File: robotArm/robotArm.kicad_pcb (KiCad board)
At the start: 4 copper layers, 127 x 66 mm, 30 parts, among them J1 Barrel_Jack, J2 Conn_01x16_Pin, J3 Conn_01x04, J4 Conn_01x04, J5 Conn_01x04, J6 Conn_01x04, U2 TMC2209_SILENTSTEPSTICK, U4 TMC2209_SILENTSTEPSTICK, U5 TMC2209_SILENTSTEPSTICK, U6 74HC165

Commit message: First Real Cleanup
First real cleanup
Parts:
- added D10: ST1, LED_THT:LED_D3.0mm_FlatTop, F.Cu at (138.4, 64.8)
- added D11: ST2, LED_THT:LED_D3.0mm_FlatTop, F.Cu at (133.3, 64.8)
- added D12: ST3, LED_THT:LED_D3.0mm_FlatTop, F.Cu at (128.3, 64.8)
- added D13: USR0, LED_THT:LED_D3.0mm_FlatTop, F.Cu at (123.2, 64.8)
- added D14: USR1, LED_THT:LED_D3.0mm_FlatTop, F.Cu at (118.1, 64.8)
- added D15: USR2, LED_THT:LED_D3.0mm_FlatTop, F.Cu at (113.0, 64.8)
- added D16: USR3, LED_THT:LED_D3.0mm_FlatTop, F.Cu at (108.0, 64.8)
- added D9: ST0, LED_THT:LED_D3.0mm_FlatTop, F.Cu at (143.5, 64.8)
- added R10: 330, Resistor_THT:R_Box_L8.4mm_W2.5mm_P5.08mm, F.Cu at (144.8, 74.9)
- added R11: 330, Resistor_THT:R_Box_L8.4mm_W2.5mm_P5.08mm, F.Cu at (139.7, 74.9)
- added R12: 330, Resistor_THT:R_Box_L8.4mm_W2.5mm_P5.08mm, F.Cu at (134.6, 74.9)
- added R13: 330, Resistor_THT:R_Box_L8.4mm_W2.5mm_P5.08mm, F.Cu at (129.5, 74.9)
- added R14: 330, Resistor_THT:R_Box_L8.4mm_W2.5mm_P5.08mm, F.Cu at (124.5, 69.8)
- added R15: 330, Resistor_THT:R_Box_L8.4mm_W2.5mm_P5.08mm, F.Cu at (119.4, 69.9)
- added R16: 330, Resistor_THT:R_Box_L8.4mm_W2.5mm_P5.08mm, F.Cu at (114.3, 69.8)
- added R17: 330, Resistor_THT:R_Box_L8.4mm_W2.5mm_P5.08mm, F.Cu at (109.2, 74.9)
- D5: value D5 -> IX1
- R2: value R -> 330
- moved U7 6.48 mm to (88.4, 89.4)
- moved J2 5.08 mm to (147.3, 78.7)
- moved U4 3.81 mm to (130.8, 83.8)
- moved U5 2.54 mm to (130.8, 108.0)
- moved U6 2.54 mm to (106.7, 83.8)
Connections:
- J2 pad 1: D0 -> ES0
- J2 pad 11: D5 -> USR1
- J2 pad 13: D6 -> USR2
- J2 pad 15: D7 -> USR3
- J2 pad 3: D1 -> ES1
- J2 pad 5: D2 -> ES2
- J2 pad 7: D3 -> ES3
- J2 pad 9: D4 -> USR0
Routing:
- net +3.3V: track 313.4 -> 236.0 mm, vias 0 -> 1
- net D0: track 48.0 -> 0.00 mm, vias 1 -> 0
- net DIR_2: track 64.2 -> 105.4 mm, vias 1 -> 0
- net D1: track 40.5 -> 0.00 mm, vias 1 -> 0
- net D2: track 34.2 -> 0.00 mm, vias 1 -> 0
- net D4: track 29.4 -> 0.00 mm, vias 1 -> 0
- net D3: track 28.8 -> 0.00 mm
- net D5: track 27.5 -> 0.00 mm, vias 1 -> 0
- net D7: track 24.1 -> 0.00 mm
- net D6: track 23.3 -> 0.00 mm
- net +12V: track 182.6 -> 167.4 mm
- net /M2-2A: track 6.89 -> 19.1 mm
- net /M4-1A: track 17.7 -> 6.35 mm
- net CLK: track 49.2 -> 38.2 mm, vias 1 -> 0
- net Net-(D9-K): track 0.00 -> 10.7 mm
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- added copper zone on In1.Cu, net +3.3V
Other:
- board size 127 x 66 mm -> 127 x 69.9 mm

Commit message: Attempt 2.1
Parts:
- removed D10: ST1, LED_THT:LED_D3.0mm_FlatTop
- removed D11: ST2, LED_THT:LED_D3.0mm_FlatTop
- removed D12: ST3, LED_THT:LED_D3.0mm_FlatTop
- removed D13: USR0, LED_THT:LED_D3.0mm_FlatTop
- removed D14: USR1, LED_THT:LED_D3.0mm_FlatTop
- removed D15: USR2, LED_THT:LED_D3.0mm_FlatTop
- removed D16: USR3, LED_THT:LED_D3.0mm_FlatTop
- added C1: 47μ, Capacitor_THT:CP_Radial_D5.0mm_P2.50mm, F.Cu at (113.7, 60.3)
- added C2: 47μ, Capacitor_THT:CP_Radial_D5.0mm_P2.50mm, F.Cu at (134.7, 128.9)
- added C3: 47μ, Capacitor_THT:CP_Radial_D5.0mm_P2.50mm, F.Cu at (136.0, 67.3)
- added C4: 100μ, Capacitor_THT:CP_Radial_D7.5mm_P2.50mm, F.Cu at (57.8, 69.8)
- added C5: 47μ, Capacitor_THT:CP_Radial_D5.0mm_P2.50mm, F.Cu at (137.2, 97.8)
- added SW1: SW_DIP_x08, Package_DIP:DIP-16_W7.62mm, F.Cu at (95.3, 109.2)
- added SW2: SW_SPDT, Library:SS-12D10G5_XKB, F.Cu at (41.9, 71.1)
- added U3: 74HC245, Package_DIP:DIP-20_W7.62mm, F.Cu at (140.3, 94.6)
- added U9: 74LS279, Package_DIP:DIP-16_W7.62mm, F.Cu at (140.3, 121.3)
- D1: value DIAG1 -> USR3; footprint LED_THT:LED_D3.0mm_FlatTop -> LED_THT:LED_D5.0mm
- D2: value DIAG2 -> USR2; footprint LED_THT:LED_D3.0mm_FlatTop -> LED_THT:LED_D5.0mm
- D3: value DIAG3 -> USR1; footprint LED_THT:LED_D3.0mm_FlatTop -> LED_THT:LED_D5.0mm
- D4: value DIAG4 -> USR0; footprint LED_THT:LED_D3.0mm_FlatTop -> LED_THT:LED_D5.0mm
- D5: value IX1 -> ES3; footprint LED_THT:LED_D3.0mm_FlatTop -> LED_THT:LED_D5.0mm
- D6: value IX2 -> ES2; footprint LED_THT:LED_D3.0mm_FlatTop -> LED_THT:LED_D5.0mm
- D7: value IX3 -> ES1; footprint LED_THT:LED_D3.0mm_FlatTop -> LED_THT:LED_D5.0mm
- D8: value IX4 -> ES0; footprint LED_THT:LED_D3.0mm_FlatTop -> LED_THT:LED_D5.0mm
- D9: value ST0 -> LED; footprint LED_THT:LED_D3.0mm_FlatTop -> LED_THT:LED_D5.0mm_Clear
- J2: value Conn_01x16_Pin -> ENDSTOP INPUTS
- J3: value Conn_01x04 -> STEPPER1
- J4: value Conn_01x04 -> STEPPER4
- J5: value Conn_01x04 -> STEPPER2
- J6: value Conn_01x04 -> STEPPER3
- R1: value R -> 470 Ω; footprint Resistor_THT:R_Axial_DIN0204_L3.6mm_D1.6mm_P2.54mm_Vertical -> Resistor_THT:R_Axial_DIN0207_L6.3mm_D2.5mm_P2.54mm_Vertical
- R10, R11, R12, R13, R14, R15, R16, R17: value 330 -> 330Ω; footprint Resistor_THT:R_Box_L8.4mm_W2.5mm_P5.08mm -> Resistor_THT:R_Axial_DIN0204_L3.6mm_D1.6mm_P2.54mm_Vertical
- R2, R3, R4, R5, R6, R7, R8, R9: value 330 -> 10kΩ; footprint Resistor_THT:R_Box_L8.4mm_W2.5mm_P5.08mm -> Resistor_THT:R_Axial_DIN0204_L3.6mm_D1.6mm_P2.54mm_Vertical
- U4: value TMC2209_SILENTSTEPSTICK -> TMC2209_MODULE
- U5: value TMC2209_SILENTSTEPSTICK -> TMC2209 Module
- moved D4 129.7 mm to (156.2, 83.8)
- moved D3 127.7 mm to (156.2, 74.9)
- moved D2 126.5 mm to (156.2, 66.0)
- moved D1 126.2 mm to (156.2, 57.1)
- moved D7 113.3 mm to (156.2, 108.0), turned to -90 degrees
- moved D8 109.2 mm to (156.2, 115.6), turned to -90 degrees
- moved D9 94.1 mm to (49.5, 69.8)
- moved R8 86.9 mm to (116.3, 111.8)
- moved U5 84.3 mm to (60.4, 61.6), turned to 90 degrees
- moved R1 77.6 mm to (55.9, 61.2), turned to -90 degrees
- moved R2 74.1 mm to (116.2, 80.6)
- moved U4 70.1 mm to (61.0, 90.2), turned to 90 degrees
- moved J5 64.8 mm to (75.6, 69.2), turned to 180 degrees
- moved R3 61.1 mm to (116.2, 85.7)
- moved R9 57.8 mm to (116.2, 116.2)
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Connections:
- D1 pad 2: +3.3V -> Net-(D1-A)
- D2 pad 1: Net-(D2-K) -> Net-(D1-K)
- D2 pad 2: +3.3V -> Net-(D2-A)
- D3 pad 1: Net-(D3-K) -> Net-(D1-K)
- D3 pad 2: +3.3V -> Net-(D3-A)
- D4 pad 1: Net-(D4-K) -> Net-(D1-K)
- D4 pad 2: +3.3V -> Net-(D4-A)
- D5 pad 1: Net-(D5-K) -> Net-(D1-K)
- D5 pad 2: +3.3V -> Net-(D5-A)
- D6 pad 1: Net-(D6-K) -> Net-(D1-K)
- D6 pad 2: +3.3V -> Net-(D6-A)
- D7 pad 1: Net-(D7-K) -> Net-(D1-K)
- D7 pad 2: +3.3V -> Net-(D7-A)
- D8 pad 1: Net-(D8-K) -> Net-(D1-K)
- D8 pad 2: +3.3V -> Net-(D8-A)
- D9 pad 2: +3.3V -> GND
- J1 pad 1: +12V -> Net-(J1-Pad1)
- J2 pad 1: ES0 -> /Endstop Section/ES0
- J2 pad 10: Net-(J2-Pin_10) -> GND
- J2 pad 11: USR1 -> /Endstop Section/USR1
- J2 pad 12: Net-(J2-Pin_10) -> GND
- J2 pad 13: USR2 -> /Endstop Section/USR2
- J2 pad 14: Net-(J2-Pin_10) -> GND
- J2 pad 15: USR3 -> /Endstop Section/USR3
- J2 pad 16: Net-(J2-Pin_10) -> GND
- J2 pad 2: Net-(J2-Pin_10) -> GND
- J2 pad 3: ES1 -> /Endstop Section/ES1
- J2 pad 4: Net-(J2-Pin_10) -> GND
- J2 pad 5: ES2 -> /Endstop Section/ES2
- J2 pad 6: Net-(J2-Pin_10) -> GND
- J2 pad 7: ES3 -> /Endstop Section/ES3
- J2 pad 8: Net-(J2-Pin_10) -> GND
- J2 pad 9: USR0 -> /Endstop Section/USR0
- J3 pad 1: /M1-2B -> /B2-DRV1
- J3 pad 2: /M1-2A -> /A2-DRV1
- J3 pad 3: /M1-1A -> /A1-DRV1
- J3 pad 4: /M1-1B -> /B1-DRV1
- J4 pad 1: /M4-1B -> /B2-DRV4
- J4 pad 2: /M4-2A -> /A2-DRV4
- J4 pad 3: /M4-1A -> /A1-DRV4
- J4 pad 4: Net-(J4-2B) -> /B1-DRV4
- J5 pad 1: /M2-2B -> /B2-DRV2
- J5 pad 2: /M2-2A -> /A2-DRV2
- J5 pad 3: /M2-1A -> /A1-DRV2
- J5 pad 4: /M2-1B -> /B1-DRV2
- J6 pad 1: /M3-2B -> /B2-DRV3
- J6 pad 2: /M3-2A -> /A2-DRV3
- J6 pad 3: /M3-1A -> /A1-DRV3
- J6 pad 4: /M3-1B -> /B1-DRV3
- R1 pad 1: +3.3V -> +12V
- R1 pad 2: Net-(U6-DS) -> Net-(D9-K)
- R10 pad 1: Net-(D9-K) -> Net-(U3-B7)
- R10 pad 2: ES0 -> Net-(D1-A)
- R11 pad 2: ES1 -> Net-(D2-A)
- R12 pad 2: ES2 -> Net-(D3-A)
- R13 pad 2: ES3 -> Net-(D4-A)
- R14 pad 1: Net-(D13-K) -> /EN_DRV4
- R14 pad 2: USR0 -> Net-(D5-A)
- R15 pad 1: Net-(D14-K) -> /EN_DRV3
- R15 pad 2: USR1 -> Net-(D6-A)
- R16 pad 1: Net-(D15-K) -> /EN_DRV2
- R16 pad 2: USR2 -> Net-(D7-A)
- R17 pad 1: Net-(D16-K) -> /EN_DRV1
- R17 pad 2: USR3 -> Net-(D8-A)
- R2 pad 1: Net-(D1-K) -> +3.3V
- R2 pad 2: DIAG1 -> /Endstop Section/USR3
- R3 pad 1: Net-(D2-K) -> +3.3V
- R3 pad 2: DIAG2 -> /Endstop Section/USR2
- R4 pad 1: Net-(D3-K) -> +3.3V
- R4 pad 2: DIAG3 -> /Endstop Section/USR1
- R5 pad 1: Net-(D4-K) -> +3.3V
- R5 pad 2: DIAG4 -> /Endstop Section/USR0
- R6 pad 1: Net-(D5-K) -> +3.3V
- R6 pad 2: IX1 -> /Endstop Section/ES3
- R7 pad 1: Net-(D6-K) -> +3.3V
- R7 pad 2: IX2 -> /Endstop Section/ES2
- R8 pad 1: Net-(D7-K) -> +3.3V
- R8 pad 2: IX3 -> /Endstop Section/ES1
- R9 pad 1: Net-(D8-K) -> +3.3V
- R9 pad 2: IX4 -> /Endstop Section/ES0
- U1 pad 11: unconnected-(U1-PDN-Pad11) -> GND
- U1 pad 12: UART2_TX -> unconnected-(U1-TX-Pad12)
- U1 pad 14: unconnected-(U1-MS2-Pad14) -> MS2-DRV1
- U1 pad 15: unconnected-(U1-MS1-Pad15) -> MS1-DRV1
- U1 pad 16: EN_DRV -> /EN_DRV1
- U1 pad 3: /M1-1B -> /B2-DRV1
- U1 pad 4: /M1-1A -> /B1-DRV1
- U1 pad 5: /M1-2A -> /A1-DRV1
- U1 pad 6: /M1-2B -> /A2-DRV1
- U2 pad 11: unconnected-(U2-PDN-Pad11) -> GND
- U2 pad 12: UART2_TX -> unconnected-(U2-TX-Pad12)
- U2 pad 14: unconnected-(U2-MS2-Pad14) -> MS2-DRV3
- U2 pad 15: +3.3V -> MS1-DRV3
- U2 pad 16: EN_DRV -> /EN_DRV3
- U2 pad 3: /M3-1B -> /B2-DRV3
- U2 pad 4: /M3-1A -> /B1-DRV3
- U2 pad 5: /M3-2A -> /A1-DRV3
- U2 pad 6: /M3-2B -> /A2-DRV3
- U4 pad 11: unconnected-(U4-PDN-Pad11) -> GND
- U4 pad 12: UART2_TX -> unconnected-(U4-TX-Pad12)
- U4 pad 14: +3.3V -> MS1-DRV4
- U4 pad 15: +3.3V -> MS2-DRV4
- U4 pad 16: EN_DRV -> /EN_DRV4
- U4 pad 3: Net-(J4-2B) -> /B2-DRV4
- U4 pad 4: /M4-1A -> /B1-DRV4
- U4 pad 5: /M4-2A -> /A1-DRV4
- U4 pad 6: /M4-1B -> /A2-DRV4
- U5 pad 11: unconnected-(U5-PDN-Pad11) -> GND
- U5 pad 12: UART2_TX -> unconnected-(U5-TX-Pad12)
- U5 pad 14: +3.3V -> MS2-DRV2
- U5 pad 15: unconnected-(U5-MS1-Pad15) -> MS1-DRV2
- U5 pad 16: EN_DRV -> /EN_DRV2
- U5 pad 3: /M2-1B -> /B2-DRV2
- U5 pad 4: /M2-1A -> /B1-DRV2
- U5 pad 5: /M2-2A -> /A1-DRV2
- U5 pad 6: /M2-2B -> /A2-DRV2
- U6 pad 10: Net-(U6-DS) -> GND
- U6 pad 11: D0 -> /Endstop Section/ES0
- U6 pad 12: D1 -> /Endstop Section/ES1
- U6 pad 13: D2 -> /Endstop Section/ES2
- U6 pad 14: D3 -> /Endstop Section/ES3
- U6 pad 3: D4 -> /Endstop Section/USR0
- U6 pad 4: D5 -> /Endstop Section/USR1
- U6 pad 5: D6 -> /Endstop Section/USR2
- U6 pad 6: D7 -> /Endstop Section/USR3
- U7 pad 20: EN_DRV -> /RESET_DRV
- U7 pad 22: UART2_TX -> unconnected-(U7-GPIO17-Pad22)
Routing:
- net +3.3V: track 236.0 -> 0.00 mm, vias 1 -> 0
- net /EN_DRV2: track 0.00 -> 150.3 mm, vias 0 -> 3
- net EN_DRV: track 137.6 -> 0.00 mm
- net UART2_TX: track 134.4 -> 0.00 mm, vias 1 -> 0
- net /EN_DRV1: track 0.00 -> 130.1 mm, vias 0 -> 2
- net /RESET_DRV: track 0.00 -> 118.3 mm
- net /EN_DRV4: track 0.00 -> 106.6 mm, vias 0 -> 1
- net MS1-DRV2: track 0.00 -> 105.5 mm, vias 0 -> 2
- net LOAD: track 35.0 -> 130.0 mm, vias 0 -> 1
- net MS2-DRV2: track 0.00 -> 93.7 mm, vias 0 -> 2
- net DATA: track 15.5 -> 108.7 mm, vias 0 -> 1
- net /Endstop Section/ES3: track 0.00 -> 85.9 mm, vias 0 -> 2
- net /EN_DRV3: track 0.00 -> 84.9 mm, vias 0 -> 2
- net /Endstop Section/ES0: track 0.00 -> 84.1 mm, vias 0 -> 1
- net /Endstop Section/ES1: track 0.00 -> 84.0 mm, vias 0 -> 2
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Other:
- board size 127 x 69.9 mm -> 127.6 x 90.2 mm
- board text added: "16"
- board text added: "74HC165"
- board text added: "74HC245"
- board text added: "74HC279"
- board text added: "8xDIP SW"
- board text added: "9"
- board text added: "Aj26 V 3.2"
- board text added: "DRV1"
- board text added: "DRV2"
- board text added: "DRV3"
- board text added: "DRV4"
- board text added: "ES0"
- board text added: "ES1"
- board text added: "ES2"
- board text added: "ES3"
- board text added: "ESP32 Devkit v1"
- board text added: "MS1"
- board text added: "MS2"
- board text added: "Robot Control Board Rev 2.0 BL (C) 2026 Turnimator Cyberdelix Jan Atle Ramsli"
- board text added: "TMC2209"
- board text added: "USR0"
- board text added: "USR1"
- board text added: "USR2"
- board text added: "USR3"
- board text removed: "12VDC"
- board text removed: "4DoF Robot Control (C) Turnimator Cyberdelix 2026 Jan Atle Ramsli"
- board text removed: "DIAG1"
- board text removed: "DIAG2"
- board text removed: "DIAG3"
- board text removed: "DIAG4"

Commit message: JLCPCB READY
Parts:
- added C6: 100µF 100V, Capacitor_THT:CP_Radial_D12.5mm_P2.50mm, F.Cu at (83.9, 71.1)
- SW2: value SW_SPDT -> ~; footprint Library:SS-12D10G5_XKB -> myBoard:K23D05 G6
- moved SW2 5.46 mm to (37.7, 74.6)
- moved J6 3.18 mm to (104.2, 99.7)
- moved U2 3.18 mm to (89.0, 93.3)
- moved U4 3.18 mm to (61.0, 93.3)
- moved J4 3.18 mm to (76.2, 99.7)
- moved J5 1.75 mm to (74.9, 67.6)
- moved J3 1.74 mm to (103.4, 67.9)
- moved U8 0.64 mm to (53.8, 101.9)
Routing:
- net /EN_DRV2: track 150.3 -> 0.00 mm, vias 3 -> 0
- net +12V: track 149.6 -> 0.00 mm
- net /EN_DRV1: track 130.1 -> 0.00 mm, vias 2 -> 0
- net LOAD: track 130.0 -> 0.00 mm, vias 1 -> 0
- net /RESET_DRV: track 118.3 -> 0.00 mm
- net CLK: track 114.5 -> 0.00 mm, vias 1 -> 0
- net STEP_1: track 112.5 -> 0.00 mm, vias 1 -> 0
- net DATA: track 108.7 -> 0.00 mm, vias 1 -> 0
- net DIR_1: track 107.7 -> 0.00 mm, vias 1 -> 0
- net /EN_DRV4: track 106.6 -> 0.00 mm, vias 1 -> 0
- net MS1-DRV2: track 105.5 -> 0.00 mm, vias 2 -> 0
- net MS2-DRV2: track 93.7 -> 0.00 mm, vias 2 -> 0
- net STEP_3: track 90.2 -> 0.00 mm, vias 1 -> 0
- net DIR_3: track 89.6 -> 0.00 mm, vias 1 -> 0
- net /Endstop Section/ES3: track 85.9 -> 0.00 mm, vias 2 -> 0
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
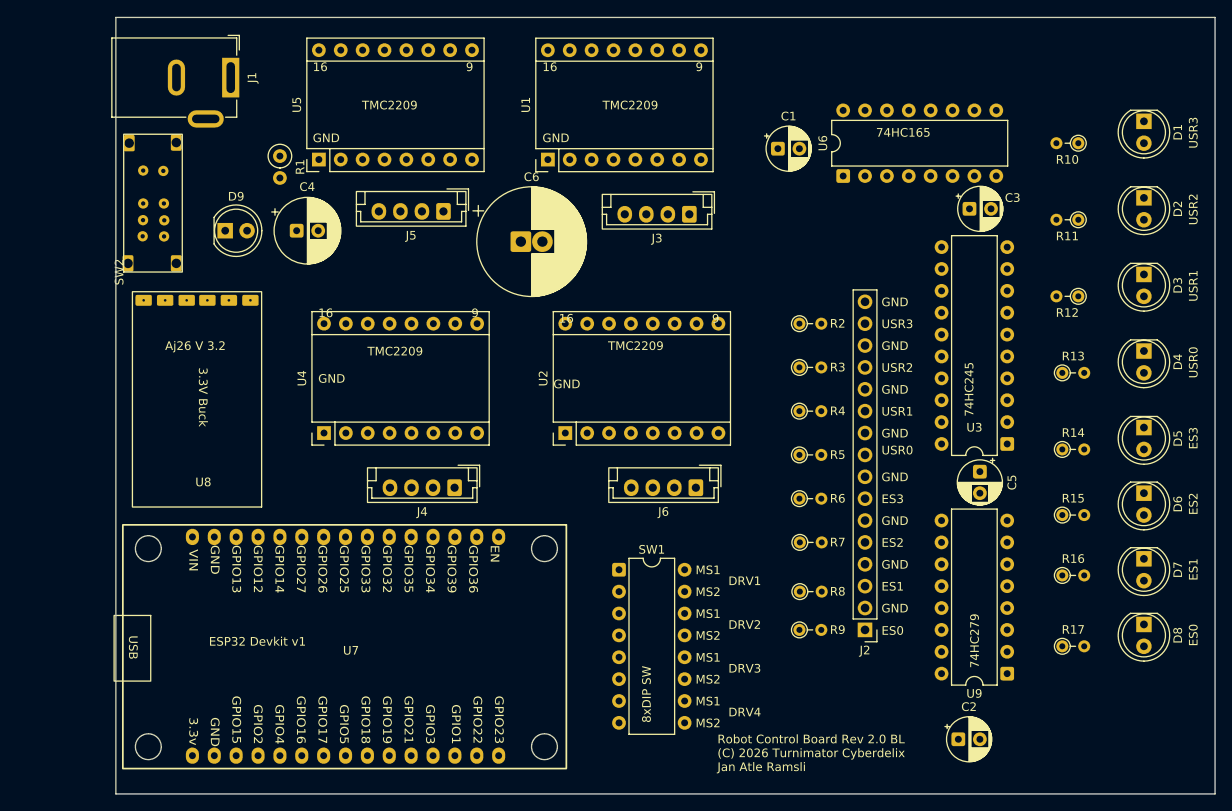
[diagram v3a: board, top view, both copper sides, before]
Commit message: Moved switch off board.
I send this off to JLCPCB.
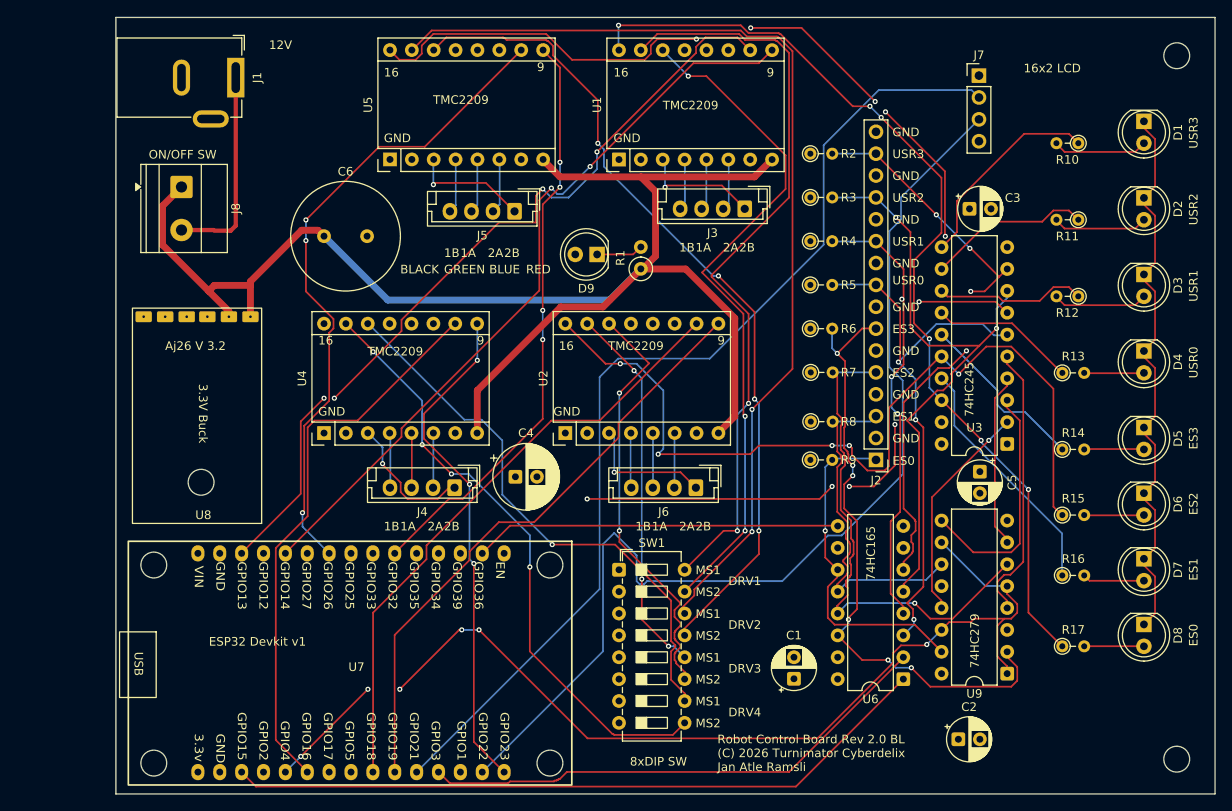
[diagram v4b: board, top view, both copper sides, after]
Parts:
- removed SW2: ~, myBoard:K23D05 G6
- added J7: Conn_01x04_Pin, Connector_PinHeader_2.54mm:PinHeader_1x04_P2.54mm_Vertical, F.Cu at (137.1, 51.8)
- added J8: Screw_Terminal_01x02, TerminalBlock_Phoenix:TerminalBlock_Phoenix_MKDS-1,5-2_1x02_P5.00mm_Horizontal, F.Cu at (44.5, 64.8)
- C6: footprint Capacitor_THT:CP_Radial_D12.5mm_P2.50mm -> Capacitor_THT:C_Radial_D12.5mm_H20.0mm_P5.00mm
- SW1: footprint Package_DIP:DIP-16_W7.62mm -> Button_Switch_THT:SW_DIP_SPSTx08_Slide_6.7x21.88mm_W7.62mm_P2.54mm_LowProfile
- moved C1 61.6 mm to (115.6, 121.9), turned to 90 degrees
- moved U6 58.8 mm to (128.3, 121.9), turned to 180 degrees
- moved R1 43.9 mm to (97.8, 74.3), turned to 90 degrees
- moved D9 43.3 mm to (92.7, 72.6), turned to 180 degrees
- moved C4 38.2 mm to (83.2, 98.4)
- moved C6 22.9 mm to (61.0, 70.5)
- moved R4 19.8 mm to (117.5, 71.1)
- moved R5 19.8 mm to (117.5, 76.1)
- moved R6 19.8 mm to (117.5, 81.2)
- moved R8 19.8 mm to (117.5, 92.0)
- moved J2 19.8 mm to (125.1, 96.5)
- moved R2 19.8 mm to (117.5, 60.9)
- moved R3 19.8 mm to (117.5, 66.0)
- moved R7 19.8 mm to (117.5, 86.3)
- moved R9 19.8 mm to (117.5, 96.5)
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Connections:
- U7 pad 21: unconnected-(U7-GPIO16-Pad21) -> STEP_4
- U7 pad 26: unconnected-(U7-GPIO21-Pad26) -> SDA
- U7 pad 29: STEP_4 -> SCL
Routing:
- net +12V: track 0.00 -> 178.1 mm
- net /EN_DRV2: track 0.00 -> 130.4 mm, vias 0 -> 5
- net /RESET_DRV: track 0.00 -> 124.1 mm, vias 0 -> 6
- net SCL: track 0.00 -> 123.3 mm
- net SDA: track 0.00 -> 119.6 mm
- net MS1-DRV2: track 0.00 -> 116.8 mm, vias 0 -> 2
- net /EN_DRV4: track 0.00 -> 114.3 mm, vias 0 -> 4
- net /EN_DRV1: track 0.00 -> 110.5 mm, vias 0 -> 6
- net /EN_DRV3: track 0.00 -> 98.8 mm, vias 0 -> 5
- net MS2-DRV2: track 0.00 -> 97.4 mm, vias 0 -> 4
- net STEP_1: track 0.00 -> 94.4 mm, vias 0 -> 4
- net MS1-DRV1: track 0.00 -> 88.4 mm, vias 0 -> 2
- net DIR_1: track 0.00 -> 88.0 mm, vias 0 -> 2
- net LOAD: track 0.00 -> 82.8 mm
- net MS2-DRV1: track 0.00 -> 78.9 mm, vias 0 -> 3
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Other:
- outline, holes or cut-outs redrawn
- board text added: "12V"
- board text added: "16x2 LCD"
- board text added: "1A"
- board text added: "1B"
- board text added: "2A"
- board text added: "2B"
- board text added: "BLACK"
- board text added: "BLUE"
- board text added: "GREEN"
- board text added: "ON/OFF SW"
- board text added: "RED"

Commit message: Added END-EFFECTOR
Not yet sent to JLCPCB
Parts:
- added J9: END EFFECTOR, Connector_PinHeader_2.54mm:PinHeader_2x05_P2.54mm_Vertical, F.Cu at (59.7, 50.2)
- C6: footprint Capacitor_THT:C_Radial_D12.5mm_H20.0mm_P5.00mm -> Capacitor_THT:C_Radial_D6.3mm_H11.0mm_P2.50mm
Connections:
- U7 pad 22: unconnected-(U7-GPIO17-Pad22) -> GPIO17
- U7 pad 6: unconnected-(U7-GPIO27-Pad6) -> GPIO27
- U7 pad 8: unconnected-(U7-GPIO25-Pad8) -> GPIO25
- U7 pad 9: unconnected-(U7-GPIO33-Pad9) -> GPIO33
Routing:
- net GPIO17: track 0.00 -> 84.3 mm
- net GPIO25: track 0.00 -> 60.7 mm
- net GPIO27: track 0.00 -> 50.7 mm
- net GPIO33: track 0.00 -> 50.0 mm
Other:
- board text added: "17"
- board text added: "25"
- board text added: "27"
- board text added: "3.3V"
- board text added: "33"
- board text added: "GPIO"
- board text added: "SCL"
- board text added: "SDA"

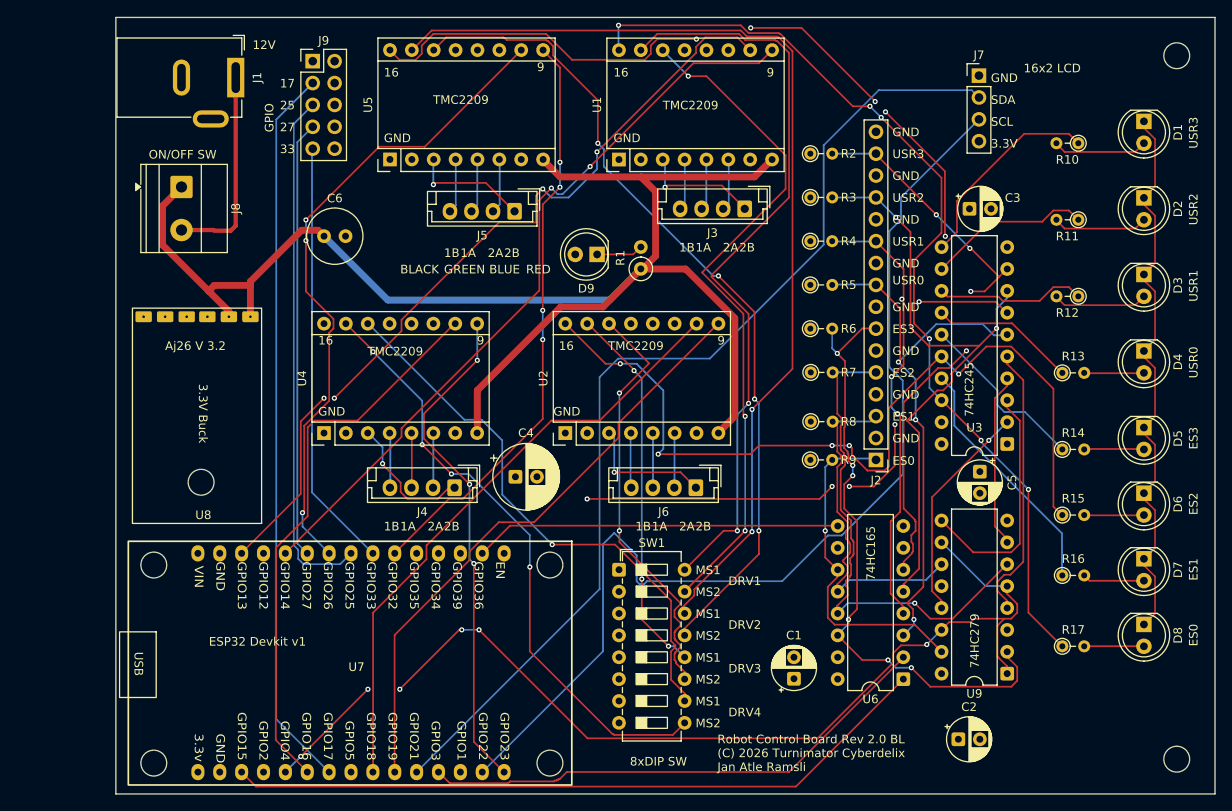
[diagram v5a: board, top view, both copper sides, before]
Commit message: Sent to JLCPCB
This is the third attempt. Modules corret, PS plug and on/off switch.
Drivers for LEDs.
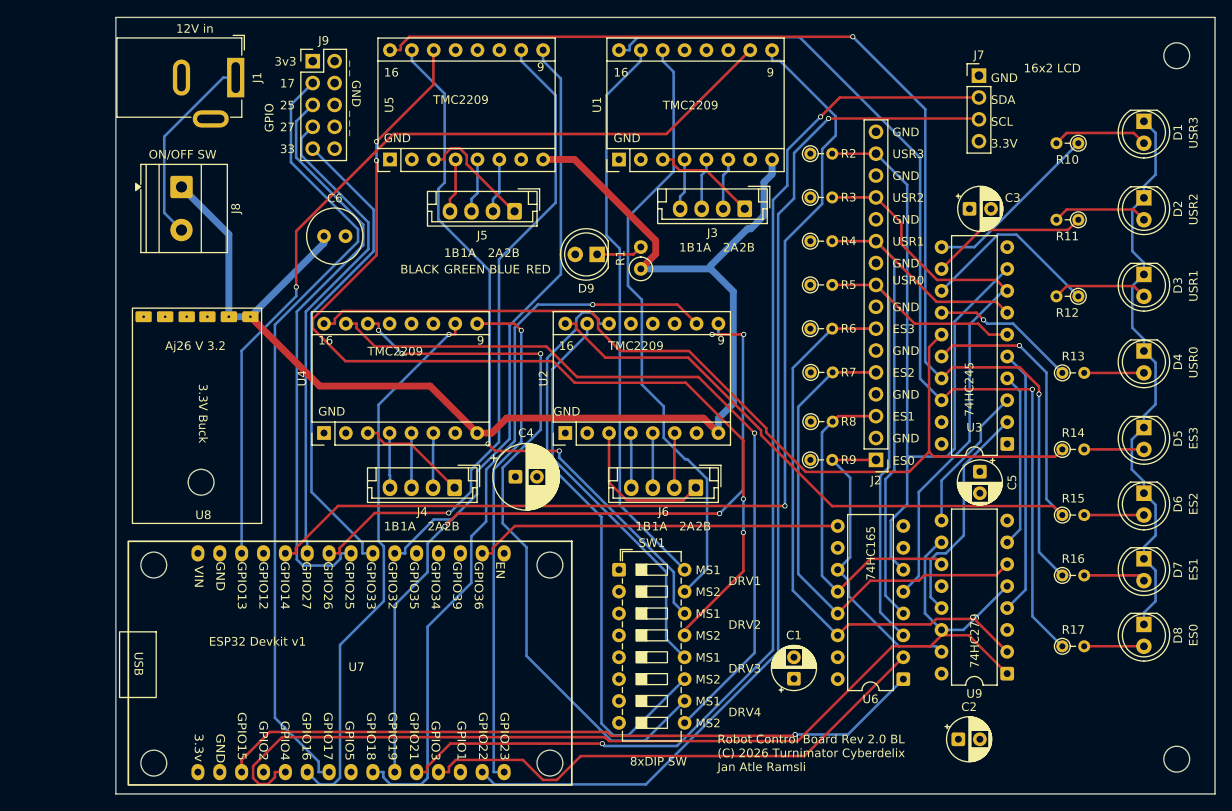
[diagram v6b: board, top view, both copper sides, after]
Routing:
- net MS1-DRV2: track 116.8 -> 83.7 mm
- net DIR_1: track 88.0 -> 119.6 mm, vias 2 -> 1
- net MS1-DRV1: track 88.4 -> 65.7 mm, vias 2 -> 0
- net MS2-DRV2: track 97.4 -> 118.8 mm
- net DIR_3: track 70.1 -> 91.1 mm, vias 0 -> 4
- net MS2-DRV3: track 49.5 -> 68.9 mm, vias 2 -> 0
- net MS2-DRV4: track 70.6 -> 90.0 mm, vias 4 -> 1
- net MS1-DRV4: track 65.0 -> 84.4 mm, vias 1 -> 3
- net +12V: track 178.1 -> 160.0 mm
- net /Endstop Section/USR3: track 68.1 -> 85.6 mm, vias 4 -> 0
- net STEP_3: track 71.0 -> 87.2 mm, vias 0 -> 1
- net SDA: track 119.6 -> 131.4 mm, vias 0 -> 2
- net Net-(U3-A1): track 28.7 -> 17.1 mm
- net MS2-DRV1: track 78.9 -> 70.6 mm, vias 3 -> 0
- net GPIO17: track 84.3 -> 91.6 mm
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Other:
- board text added: "12V in"
- board text added: "3v3"
- board text added: "_ _ GND _ _ _"
- board text removed: "12V"
